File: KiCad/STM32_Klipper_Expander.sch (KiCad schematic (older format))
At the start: 44 parts, among them J1 USB_B_Micro, J10 Conn_01x01, J11 Conn_01x03, J12 Conn_01x02, J2 Conn_01x04, J3 Conn_02x05, J4 Conn_01x03, J5 Vin, J6 Screw_Terminal_01x08, J7 Conn_01x02, J8 Conn_01x02, J9 Conn_01x02, Q1 IRLML6344TRPBF, Q2 IRLML6344TRPBF, Q3 IRLML6344TRPBF, Q4 IRLML6344TRPBF, SW2 SW_SPST, U1 STM32F042F6Px, U2 AP2127K-3.3, U3 74LVC1G17

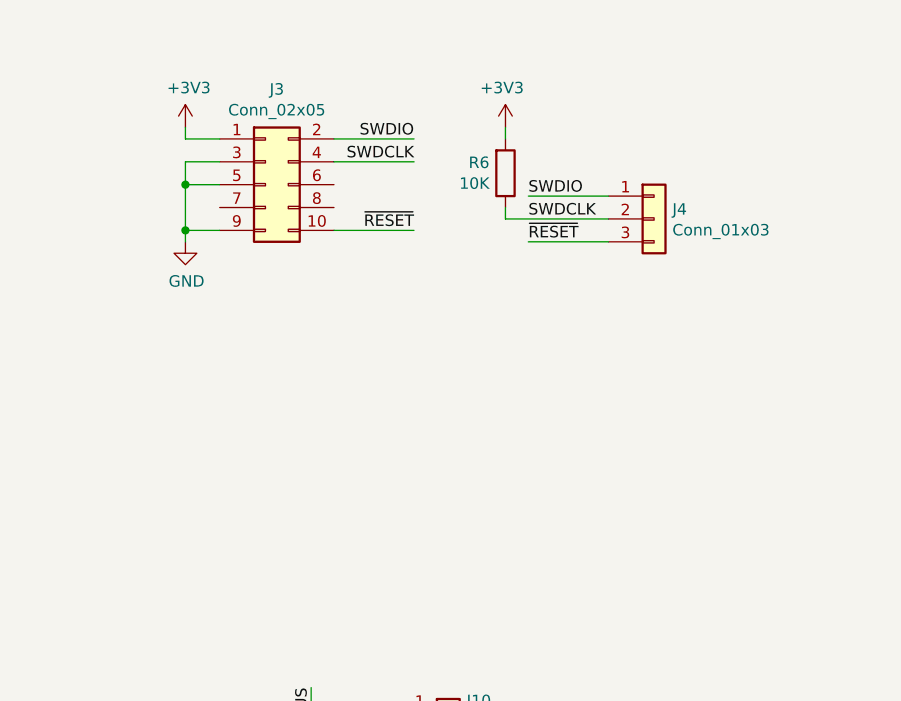
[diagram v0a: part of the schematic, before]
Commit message: Addition of mounting hole
APPARENTLY we need some way to mount this....
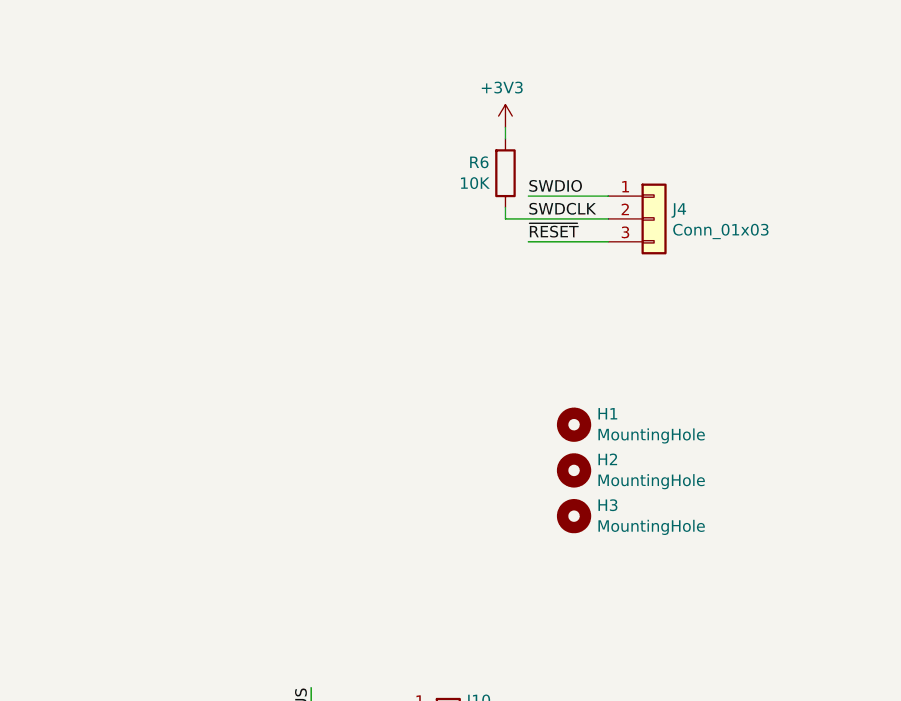
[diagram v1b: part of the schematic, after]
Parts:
- removed J3: Conn_02x05, Connector_PinHeader_1.27mm:PinHeader_2x05_P1.27mm_Vertical, symbol Connector_Generic:Conn_02x05_Odd_Even
- added H1, H2, H3: MountingHole, MountingHole:MountingHole_3.2mm_M3, symbol Mechanical:MountingHole
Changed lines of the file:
@@
 Wire Wire Line
 	1850 6500 1850 6450
-$Comp
-L Connector_Generic:Conn_02x05_Odd_Even J3
-U 1 1 5E20939C
-P 5350 1200
-F 0 "J3" H 5400 1617 50  0000 C CNN
-F 1 "Conn_02x05" H 5400 1526 50  0000 C CNN
-F 2 "Connector_PinHeader_1.27mm:PinHeader_2x05_P1.27mm_Vertical" H 5350 1200 50  0001 C CNN
-F 3 "~" H 5350 1200 50  0001 C CNN
-	1    5350 1200
-	1    0    0    -1
-$EndComp
-$Comp
-L power:GND #PWR018
-U 1 1 5E20AEF8
-P 5000 1450
-F 0 "#PWR018" H 5000 1200 50  0001 C CNN
-F 1 "GND" H 5005 1277 50  0000 C CNN
-F 2 "" H 5000 1450 50  0001 C CNN
-F 3 "" H 5000 1450 50  0001 C CNN
-	1    5000 1450
-	1    0    0    -1
-$EndComp
-Wire Wire Line
-	5150 1100 5000 1100
-Wire Wire Line
-	5000 1100 5000 1200
-Wire Wire Line
-	5150 1200 5000 1200
-Connection ~ 5000 1200
-Wire Wire Line
-	5000 1200 5000 1400
-Wire Wire Line
-	5150 1400 5000 1400
-Connection ~ 5000 1400
-Wire Wire Line
-	5000 1400 5000 1450
-Wire Wire Line
-	5150 1000 5000 1000
-Wire Wire Line
-	5000 1000 5000 950
-$Comp
-L power:+3V3 #PWR017
-U 1 1 5E21B065
-P 5000 950
-F 0 "#PWR017" H 5000 800 50  0001 C CNN
-F 1 "+3V3" H 5015 1123 50  0000 C CNN
-F 2 "" H 5000 950 50  0001 C CNN
-F 3 "" H 5000 950 50  0001 C CNN
-	1    5000 950
-	1    0    0    -1
-$EndComp
-Wire Wire Line
-	5650 1000 6000 1000
-Wire Wire Line
-	5650 1100 6000 1100
-Text Label 6000 1000 2    50   ~ 0
-SWDIO
-Text Label 6000 1100 2    50   ~ 0
-SWDCLK
-Text Label 6000 1400 2    50   ~ 0
-~RESET
-Wire Wire Line
-	5650 1400 6000 1400
 Wire Wire Line
 	6850 1250 6500 1250
@@
 Wire Wire Line
 	3950 5700 4100 5700
+$Comp
+L Mechanical:MountingHole H1
+U 1 1 5E200A2F
+P 6700 2250
+F 0 "H1" H 6800 2296 50  0000 L CNN
+F 1 "MountingHole" H 6800 2205 50  0000 L CNN
+F 2 "MountingHole:MountingHole_3.2mm_M3" H 6700 2250 50  0001 C CNN
+F 3 "~" H 6700 2250 50  0001 C CNN
+	1    6700 2250
+	1    0    0    -1
+$EndComp
+$Comp
+L Mechanical:MountingHole H2
+U 1 1 5E21A8E2
+P 6700 2450
+F 0 "H2" H 6800 2496 50  0000 L CNN
+F 1 "MountingHole" H 6800 2405 50  0000 L CNN
+F 2 "MountingHole:MountingHole_3.2mm_M3" H 6700 2450 50  0001 C CNN
+F 3 "~" H 6700 2450 50  0001 C CNN
+	1    6700 2450
+	1    0    0    -1
+$EndComp
+$Comp
+L Mechanical:MountingHole H3
+U 1 1 5E220938
+P 6700 2650
+F 0 "H3" H 6800 2696 50  0000 L CNN
+F 1 "MountingHole" H 6800 2605 50  0000 L CNN
+F 2 "MountingHole:MountingHole_3.2mm_M3" H 6700 2650 50  0001 C CNN
+F 3 "~" H 6700 2650 50  0001 C CNN
+	1    6700 2650
+	1    0    0    -1
+$EndComp
 $EndSCHEMATC

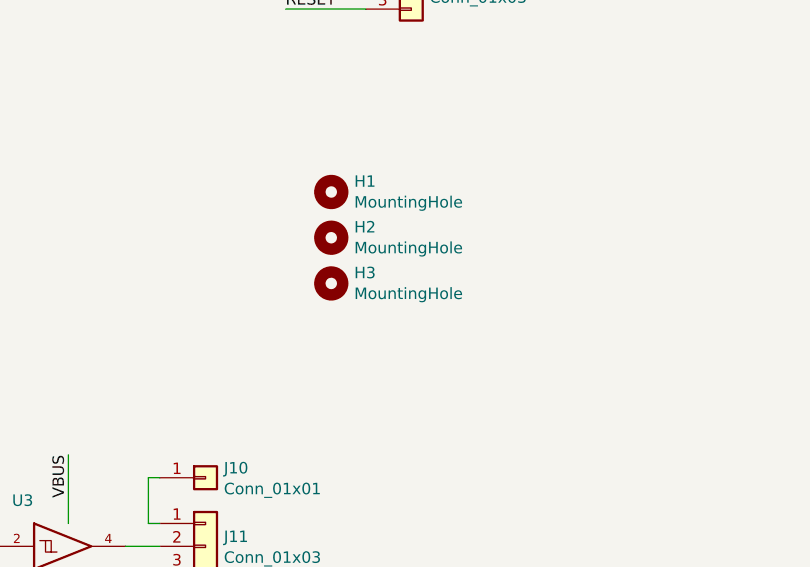
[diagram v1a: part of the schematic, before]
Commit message: Reorganization for more effiecent layout
Moving to a 100mm x 25mm PCB
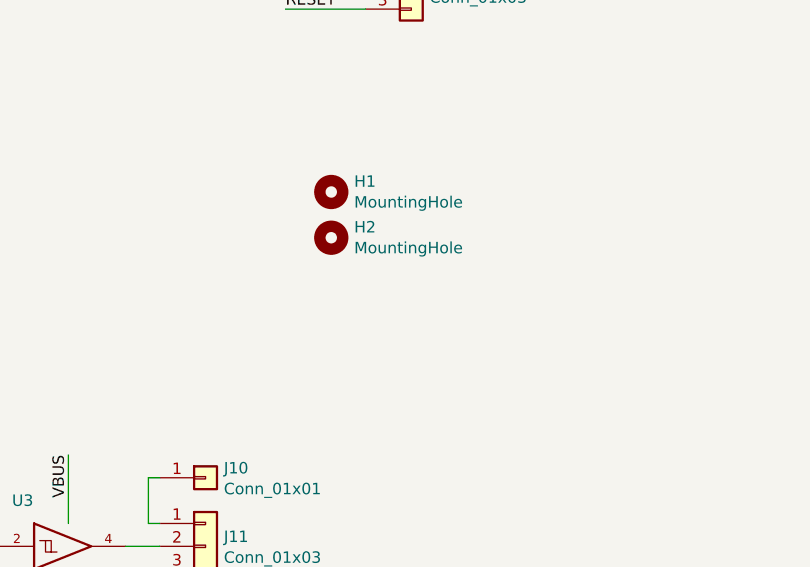
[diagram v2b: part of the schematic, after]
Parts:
- removed H3: MountingHole, MountingHole:MountingHole_3.2mm_M3, symbol Mechanical:MountingHole
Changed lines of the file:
@@
-	1    0    0    -1
-$EndComp
-$Comp
-L Mechanical:MountingHole H3
-U 1 1 5E220938
-P 6700 2650
-F 0 "H3" H 6800 2696 50  0000 L CNN
-F 1 "MountingHole" H 6800 2605 50  0000 L CNN
-F 2 "MountingHole:MountingHole_3.2mm_M3" H 6700 2650 50  0001 C CNN
-F 3 "~" H 6700 2650 50  0001 C CNN
-	1    6700 2650
 	1    0    0    -1
 $EndComp

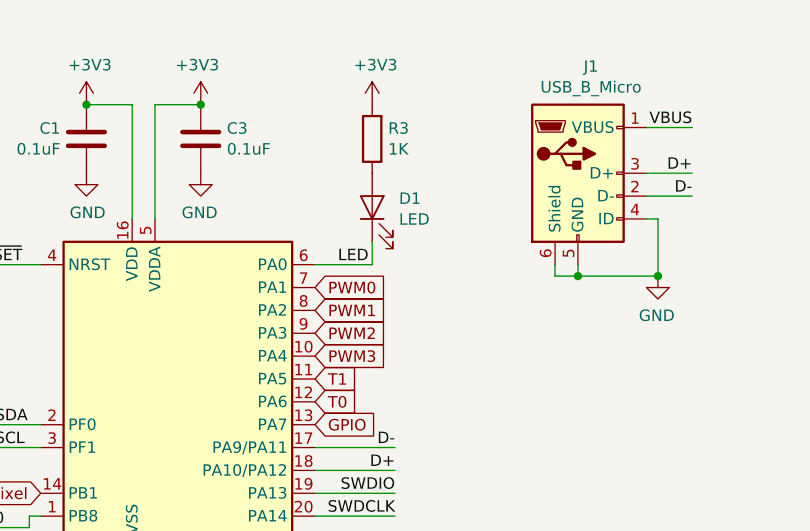
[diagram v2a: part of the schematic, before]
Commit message: Routing and finalizations
Completed routing on the thinner variant. Need to gerenate BOM and CPL files for JLCPCB assembly
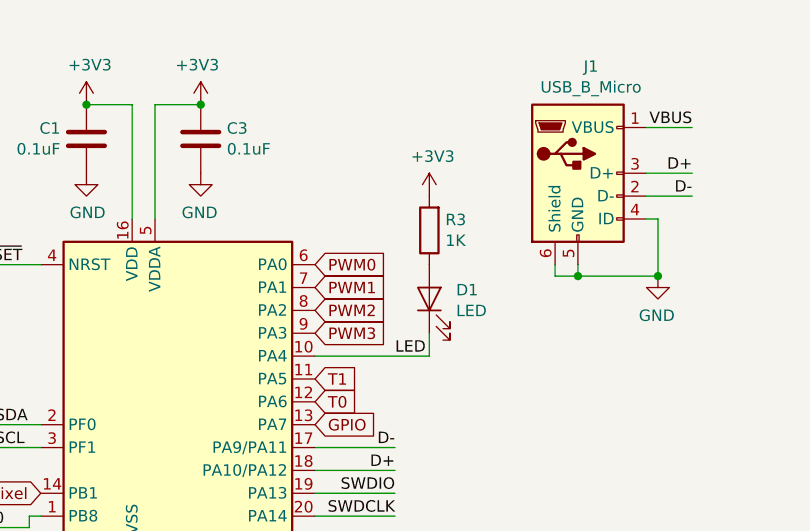
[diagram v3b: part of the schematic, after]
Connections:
- net LED: now also U1.10 (PA4); no longer U1.6 (PA0)
- net PWM0: now also U1.6 (PA0); no longer U1.7 (PA1)
- net PWM1: now also U1.7 (PA1); no longer U1.8 (PA2)
- net PWM2: now also U1.8 (PA2); no longer U1.9 (PA3)
- net PWM3: now also U1.9 (PA3); no longer U1.10 (PA4)
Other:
- moved on the sheet: D1, R3
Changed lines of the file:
@@
 	1    0    0    -1
-$EndComp
-$Comp
-L power:+3V3 #PWR012
-U 1 1 5E207BBA
-P 2600 850
-F 0 "#PWR012" H 2600 700 50  0001 C CNN
-F 1 "+3V3" H 2615 1023 50  0000 C CNN
-F 2 "" H 2600 850 50  0001 C CNN
-F 3 "" H 2600 850 50  0001 C CNN
-	1    2600 850
-	1    0    0    -1
-$EndComp
-Wire Wire Line
-	2600 1550 2600 1450
-$Comp
-L Device:LED D1
-U 1 1 5E207BFA
-P 2600 1300
-F 0 "D1" V 2639 1183 50  0000 R CNN
-F 1 "LED" V 2548 1183 50  0000 R CNN
-F 2 "LED_SMD:LED_0805_2012Metric" H 2600 1300 50  0001 C CNN
-F 3 "~" H 2600 1300 50  0001 C CNN
-	1    2600 1300
-	0    -1   -1   0
-$EndComp
-$Comp
-L Device:R R3
-U 1 1 5E207C00
-P 2600 1000
-F 0 "R3" H 2530 954 50  0000 R CNN
-F 1 "1K" H 2530 1045 50  0000 R CNN
-F 2 "Resistor_SMD:R_0805_2012Metric" V 2530 1000 50  0001 C CNN
-F 3 "~" H 2600 1000 50  0001 C CNN
-	1    2600 1000
-	-1   0    0    1
 $EndComp
 Wire Wire Line
@@
 	10000 2650 10000 2000
 Connection ~ 10000 2650
+Text GLabel 2350 1550 2    50   Input ~ 0
+PWM0
 Text GLabel 2350 1650 2    50   Input ~ 0
-PWM0
+PWM1
 Text GLabel 2350 1750 2    50   Input ~ 0
-PWM1
+PWM2
 Text GLabel 2350 1850 2    50   Input ~ 0
-PWM2
-Text GLabel 2350 1950 2    50   Input ~ 0
 PWM3
-Wire Wire Line
-	2600 1550 2350 1550
-Text Label 2450 1550 0    50   ~ 0
-LED
 Wire Wire Line
 	1250 4550 1250 4600
@@
 	1    0    0    -1
 $EndComp
+$Comp
+L power:+3V3 #PWR012
+U 1 1 5E207BBA
+P 2850 1250
+F 0 "#PWR012" H 2850 1100 50  0001 C CNN
+F 1 "+3V3" H 2865 1423 50  0000 C CNN
+F 2 "" H 2850 1250 50  0001 C CNN
+F 3 "" H 2850 1250 50  0001 C CNN
+	1    2850 1250
+	1    0    0    -1
+$EndComp
+Wire Wire Line
+	2850 1950 2850 1850
+$Comp
+L Device:LED D1
+U 1 1 5E207BFA
+P 2850 1700
+F 0 "D1" V 2889 1583 50  0000 R CNN
+F 1 "LED" V 2798 1583 50  0000 R CNN
+F 2 "LED_SMD:LED_0805_2012Metric" H 2850 1700 50  0001 C CNN
+F 3 "~" H 2850 1700 50  0001 C CNN
+	1    2850 1700
+	0    -1   -1   0
+$EndComp
+$Comp
+L Device:R R3
+U 1 1 5E207C00
+P 2850 1400
+F 0 "R3" H 2780 1354 50  0000 R CNN
+F 1 "1K" H 2780 1445 50  0000 R CNN
+F 2 "Resistor_SMD:R_0805_2012Metric" V 2780 1400 50  0001 C CNN
+F 3 "~" H 2850 1400 50  0001 C CNN
+	1    2850 1400
+	-1   0    0    1
+$EndComp
+Wire Wire Line
+	2850 1950 2350 1950
+Text Label 2700 1950 0    50   ~ 0
+LED
 $EndSCHEMATC

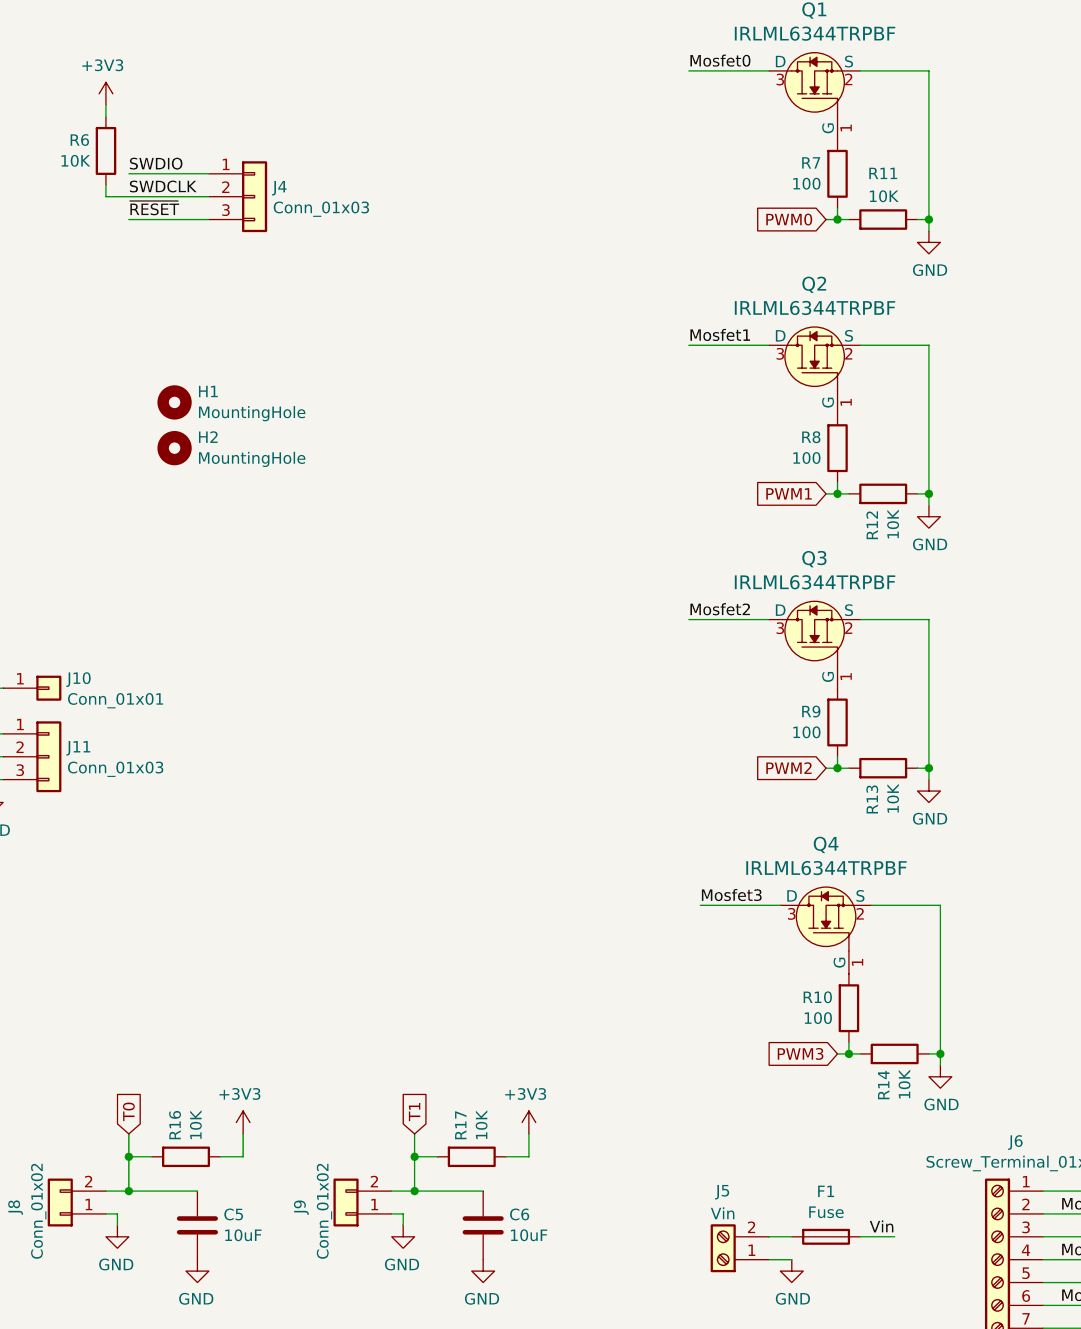
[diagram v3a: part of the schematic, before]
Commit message: Production Files
Production files created and edited for use with JLCPCB's SMT assembly.  The STM32_Klipper_Expander_CPL.csv and STM32_Klipper_Expander_BOM.csv files are used with the online tool to add the part numbers and locations to the PCB.
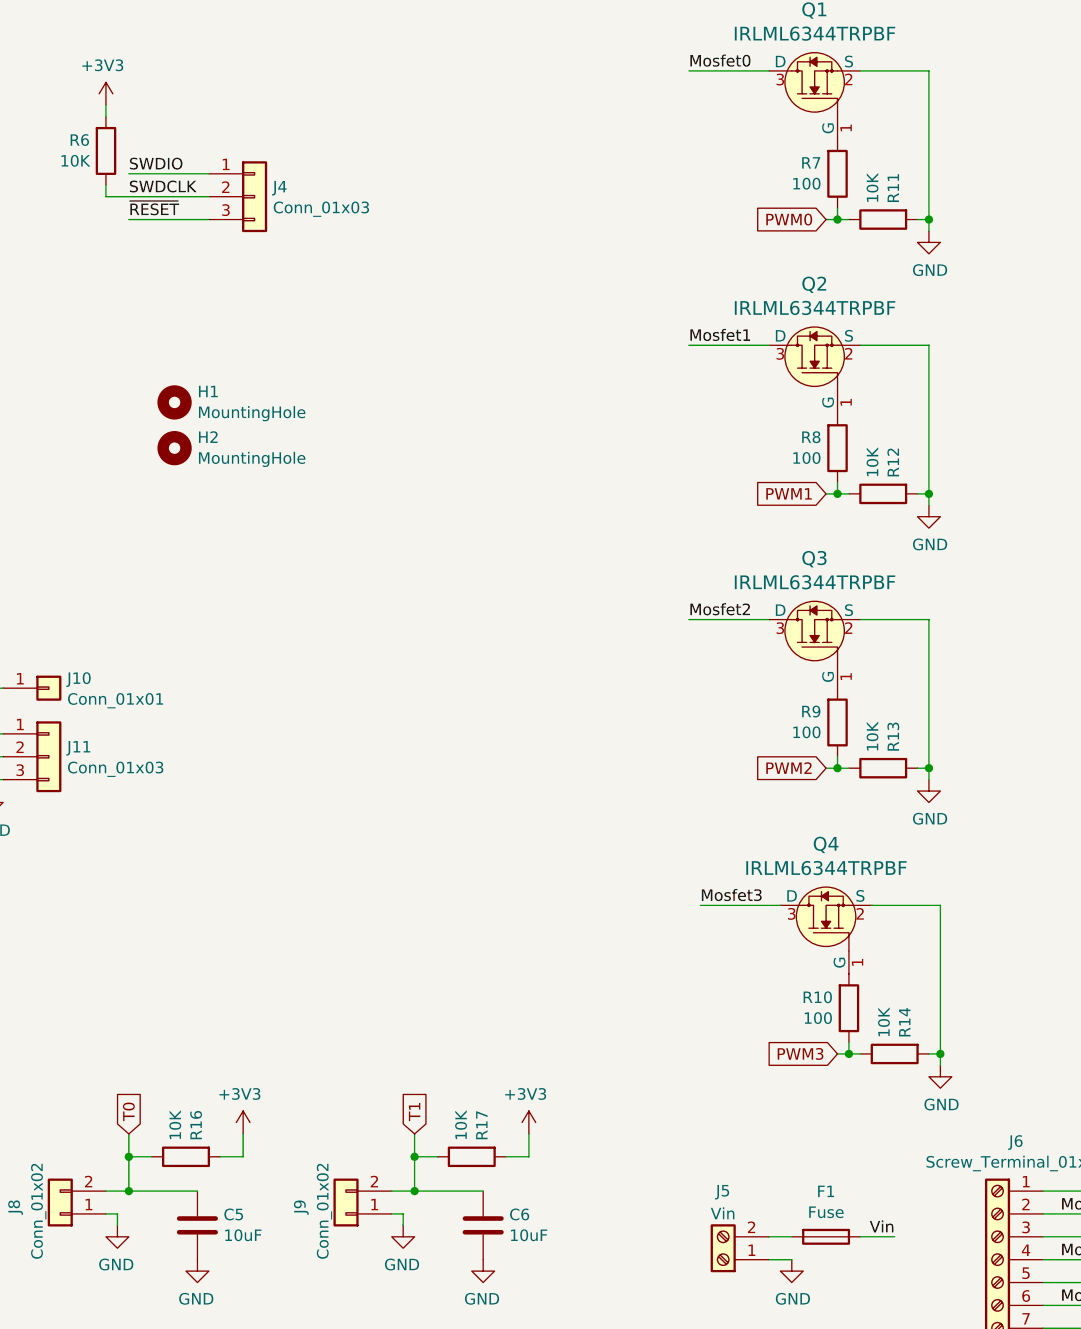
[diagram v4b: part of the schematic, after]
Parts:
- C1, C3: LCSC (none) -> C49678
- C2, C4: LCSC (none) -> C1779
- C5, C6: LCSC (none) -> C15850
- D1: LCSC (none) -> C84256
- J1: footprint Connector_USB:USB_Micro-B_Molex_47346-0001 -> TRA_KiCad_Footprints:Molex-105017-0001-USBMicroB
- Q1, Q2, Q3, Q4: LCSC (none) -> C20917
- R1, R11, R12, R13, R14, R16, R17, R2, R6: LCSC (none) -> C17414
- R10, R7, R8, R9: LCSC (none) -> C17408
- R3: LCSC (none) -> C17513
- R4, R5: LCSC (none) -> C17673
- U1: LCSC (none) -> C81000
- U2: LCSC (none) -> C156285
- U3: LCSC (none) -> C124293
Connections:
- net +3V3: now also R16.2, R17.2; no longer R16.1, R17.1
- net GND: now also R11.2, R12.2, R13.2, R14.2; no longer R11.1, R12.1, R13.1, R14.1
- net PWM0: now also R11.1; no longer R11.2
- net PWM1: now also R12.1; no longer R12.2
- net PWM2: now also R13.1; no longer R13.2
- net PWM3: now also R14.1; no longer R14.2
- net T0: now also R16.1; no longer R16.2
- net T1: now also R17.1; no longer R17.2

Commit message: Added Seeed Studio Production files
Added the Assembly files zip, Gerber zip and BOM in the neede format for SEEED studio. Can always remove the longer lead time parts to hand solder those yourselves.
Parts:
- C1, C3: MPN (none) -> CC0805KRX7R9BB104; SKU (none) -> 302010165
- C2, C4: MPN (none) -> CC0805KKX5R8BB475; SKU (none) -> 302010146
- C5, C6: MPN (none) -> CC0805ZKY5V6BB106; SKU (none) -> 302010158
- D1: MPN (none) -> 17-215SURC/S530-A2/TR8; SKU (none) -> 304090046
- J1: MPN (none) -> 1050170001
- R1, R11, R12, R13, R14, R16, R17, R2, R6: MPN (none) -> RC0805JR-0710KL; SKU (none) -> 301010361
- R10, R7, R8, R9: MPN (none) -> RC0805JR-07100RL; SKU (none) -> 301010319
- R3: MPN (none) -> RC0805JR-071KL; SKU (none) -> 301010311
- R4, R5: MPN (none) -> RC0805JR-074K7L; SKU (none) -> 301010306
- U1: MPN (none) -> STM32F042F6P6
- U2: MPN (none) -> AP2127K-3.3TRG1
- U3: MPN (none) -> 74LVC1G17SE-7
